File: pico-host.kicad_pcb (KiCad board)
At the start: 2 copper layers, 22.9 x 50.8 mm, 69 parts, among them J1 USB_C_Receptacle_USB2.0, J2 I2C, J3 USB_A, J4 Conn, J5 Conn, J6 BAT, Q1 BSS83P, SW1 SW_Push, SW2 SW_Push, U1 RP2040, U2 W25Q128JVS, U3 AP2112K-3.3, U4 MCP73831, U5 TPS61023DRLR, Y1 24MHz

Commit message: Tracks almost finished
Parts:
- Q1: footprint Package_DFN_QFN:Diodes_DFN1006-3 -> DMG3415UFY4Q-7:TRANS_DMG3415UFY4Q-7
- moved C7 19.4 mm to (150.3, 106.0)
- moved C9 19.3 mm to (151.4, 106.1)
- moved R14 17.3 mm to (150.3, 113.3)
- moved C11 16.6 mm to (149.8, 101.9)
- moved C13 14.5 mm to (151.6, 101.8), turned to -90 degrees
- moved D5 11.6 mm to (130.5, 104.5), turned to 0 degrees
- moved C6 6.15 mm to (135.5, 107.1)
- moved C16 4.72 mm to (142.3, 100.7), turned to 90 degrees
- moved R3 4.37 mm to (142.8, 102.1), turned to 180 degrees
- moved C12 4.32 mm to (143.3, 100.7), turned to 90 degrees
- moved U2 2.20 mm to (142.0, 104.9)
- moved C17 0.58 mm to (137.7, 106.6)
- moved C10 0.53 mm to (134.1, 107.4)
- moved C15 0.53 mm to (132.5, 107.5)
- moved R13 0.36 mm to (143.3, 81.2)
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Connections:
- C3 pad 1: Net-(D1-K) -> VHI
- D1 pad 1: Net-(D1-K) -> VHI
- Q1 pad 2: Net-(D1-K) -> VHI
- R9 pad 1: Net-(D1-K) -> VHI
- U3 pad 1: Net-(D1-K) -> VHI
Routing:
- net VBUS: track 6.10 -> 54.1 mm, vias 1 -> 6
- net VHI: track 6.42 -> 51.7 mm, vias 0 -> 2
- net /GPIO4: track 0.00 -> 32.3 mm, vias 0 -> 1
- net /GPIO13: track 0.00 -> 27.6 mm, vias 0 -> 2
- net /GPIO2: track 0.00 -> 26.7 mm, vias 0 -> 2
- net /GPIO0: track 0.00 -> 26.6 mm, vias 0 -> 1
- net /USB_DN: track 0.64 -> 26.5 mm, vias 1 -> 2
- net +3V3: track 13.9 -> 39.8 mm
- net /USB_DP: track 0.66 -> 25.1 mm, vias 1 -> 2
- net /GPIO1: track 0.00 -> 23.7 mm, vias 0 -> 1
- net /GPIO3: track 0.00 -> 23.5 mm, vias 0 -> 2
- net /GPIO20: track 0.00 -> 22.6 mm, vias 0 -> 1
- net /GPIO19: track 0.00 -> 21.8 mm, vias 0 -> 1
- net /GPIO18: track 1.46 -> 22.8 mm, vias 1 -> 2
- net /GPIO5: track 0.00 -> 20.6 mm, vias 0 -> 1
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
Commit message: Finished Tracks
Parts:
- removed C6: 1uF, Capacitor_SMD:C_0603_1608Metric
- C9: footprint Capacitor_SMD:C_0603_1608Metric -> Capacitor_SMD:C_0402_1005Metric
- moved C11 23.6 mm to (130.2, 88.8), turned to 0 degrees
- moved R14 20.3 mm to (132.0, 104.4), turned to 90 degrees
- moved C9 16.6 mm to (134.8, 105.4)
- moved C7 16.4 mm to (133.9, 105.4)
- moved C13 15.4 mm to (138.2, 94.3), turned to 0 degrees
- moved R1 5.48 mm to (133.3, 93.3), turned to -90 degrees
- moved C10 2.63 mm to (135.8, 105.4)
- moved C15 2.17 mm to (133.0, 105.4)
- moved D5 0.85 mm to (130.0, 103.8)
- moved C1 0.74 mm to (136.6, 88.9)
- moved C2 0.74 mm to (134.8, 88.9)
- moved C14 0.74 mm to (135.3, 93.3)
- moved C8 0.74 mm to (134.4, 93.3)
- moved R2 0.74 mm to (136.2, 93.3)
- moved Y1 0.74 mm to (135.7, 90.9)
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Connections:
- D5 pad 1: +3V3 -> /GPIO20
- D5 pad 4: /GPIO20 -> /GPIO21
- J4 pad 11: /GPIO18 -> /GPIO14
- J4 pad 12: /GPIO19 -> /GPIO15
- J4 pad 13: /GPIO20 -> /GPIO8
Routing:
- net +3V3: track 39.8 -> 110.5 mm, vias 0 -> 8
- net /GPIO8: track 0.00 -> 25.7 mm, vias 0 -> 1
- net /GPIO15: track 0.00 -> 24.6 mm, vias 0 -> 1
- net /GPIO14: track 0.00 -> 22.1 mm, vias 0 -> 1
- net /GPIO19: track 21.8 -> 0.00 mm, vias 1 -> 0
- net /GPIO20: track 22.6 -> 9.53 mm, vias 1 -> 2
- net +1V2: track 5.70 -> 16.0 mm
- net /GPIO21: track 0.00 -> 8.68 mm, vias 0 -> 2
- net /GPIO18: track 22.8 -> 28.1 mm, vias 2 -> 5
- net /~{RST}: track 16.0 -> 21.0 mm
- net /GPIO25: track 10.5 -> 14.9 mm
- net GND: track 4.63 -> 6.96 mm, vias 7 -> 49
- net /GPIO4: track 32.3 -> 30.0 mm, vias 1 -> 2
- net Net-(C2-Pad2): track 3.36 -> 5.41 mm
- net /GPIO0: track 26.6 -> 27.9 mm
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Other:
- board text added: "BOOT"
- board text removed: "BOOTSEL"

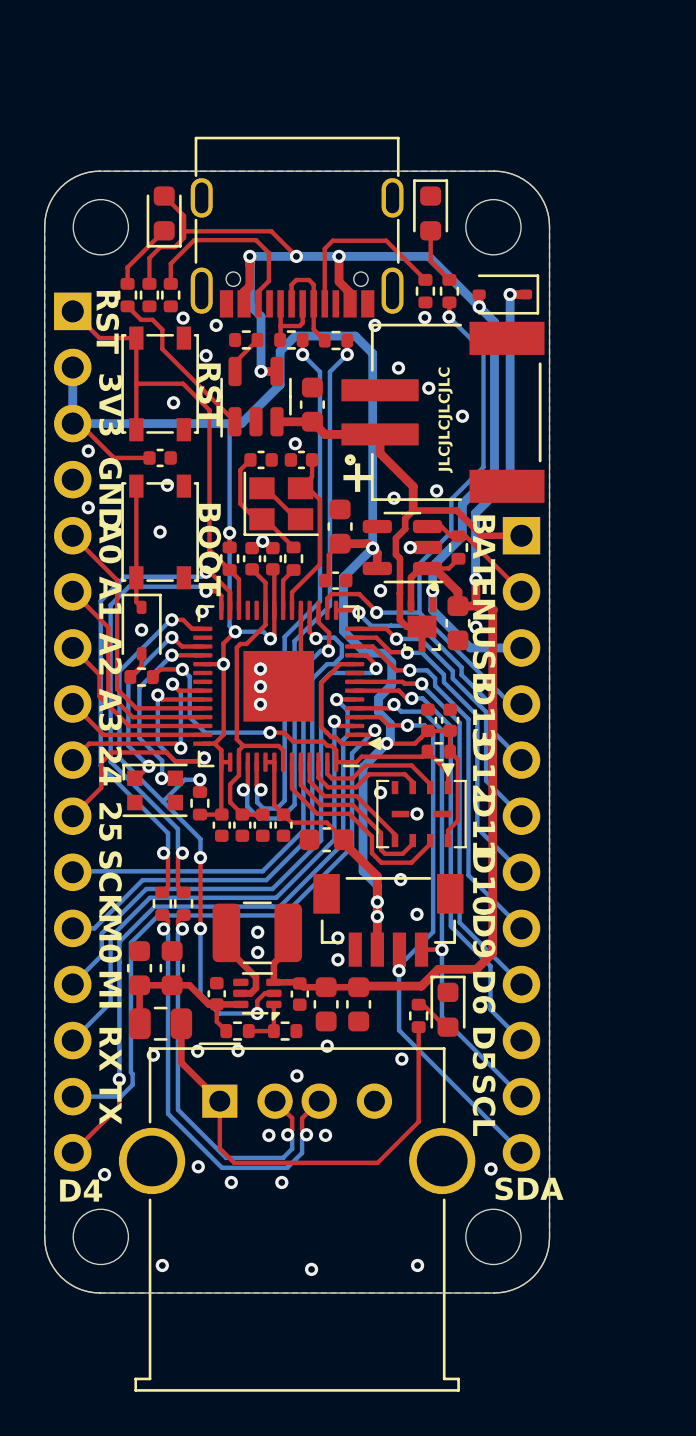
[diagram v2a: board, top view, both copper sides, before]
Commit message: Added qr logo, doc/images, updated README
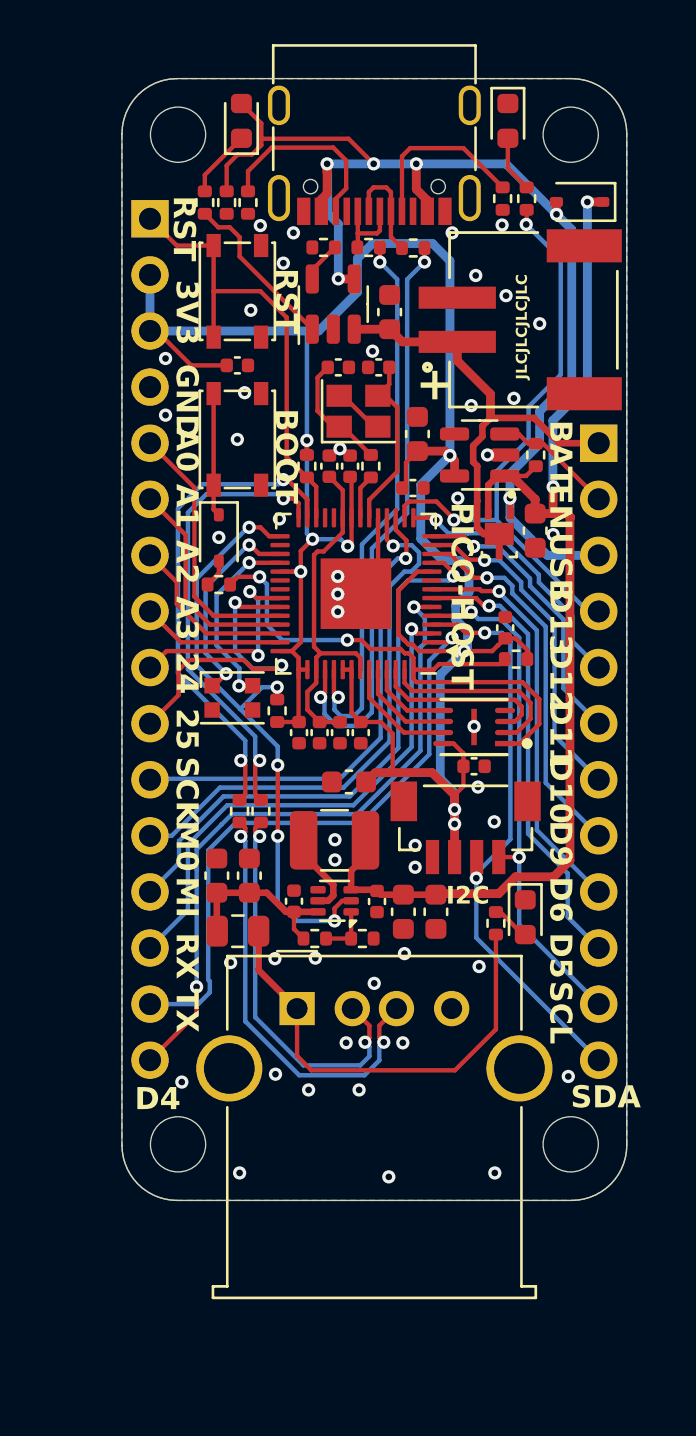
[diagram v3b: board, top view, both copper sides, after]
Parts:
- removed U2: W25Q128JVS, SPI-Flash:USON-8-3x4
- added G***: LOGO, pico-host-logo:pico-host-github-qr-15x15, B.Cu at (139.9, 97.0)
- added U6: W25Q16JVUXIQ, W25Q16JVUXIQ:Winbond-UX-0-0-IPC_B, F.Cu at (144.4, 101.0)
- moved C10 5.46 mm to (139.3, 101.2)
- moved C13 5.46 mm to (141.6, 90.1)
- moved C16 5.46 mm to (145.8, 96.5)
- moved C20 5.46 mm to (141.2, 109.3)
- moved D3 5.46 mm to (132.9, 92.4)
- moved D6 5.46 mm to (146.7, 109.6)
- moved F1 5.46 mm to (133.7, 110.2)
- moved H1 5.46 mm to (148.8, 74.1)
- moved H2 5.46 mm to (131.0, 74.1)
- moved H3 5.46 mm to (131.0, 119.9)
- moved H4 5.46 mm to (148.8, 119.9)
- moved J2 5.46 mm to (144.0, 104.3)
- moved L1 5.46 mm to (138.1, 106.1)
- moved Q1 5.46 mm to (145.6, 92.2)
- moved R1 5.46 mm to (136.8, 89.2)
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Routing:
- net /QSPI_SS: track 17.9 -> 25.5 mm
- net /QSPI_SD3: track 9.80 -> 5.28 mm
- net /QSPI_SCLK: track 8.17 -> 4.56 mm
- net /QSPI_SD1: track 6.03 -> 8.81 mm
- net /QSPI_SD2: track 5.78 -> 8.10 mm
- net /QSPI_SD0: track 6.00 -> 3.86 mm
- net +3V3: track 110.5 -> 111.0 mm
- net GND: vias 49 -> 48
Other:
- board text added: "I2C"
- board text added: "PICO-HOST"
